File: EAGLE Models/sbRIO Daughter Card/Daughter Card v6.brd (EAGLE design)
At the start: 153.7 x 102.9 mm, 96 parts, among them IC1 BTS716G, IC2 BTS716G, IC3 BTS716G

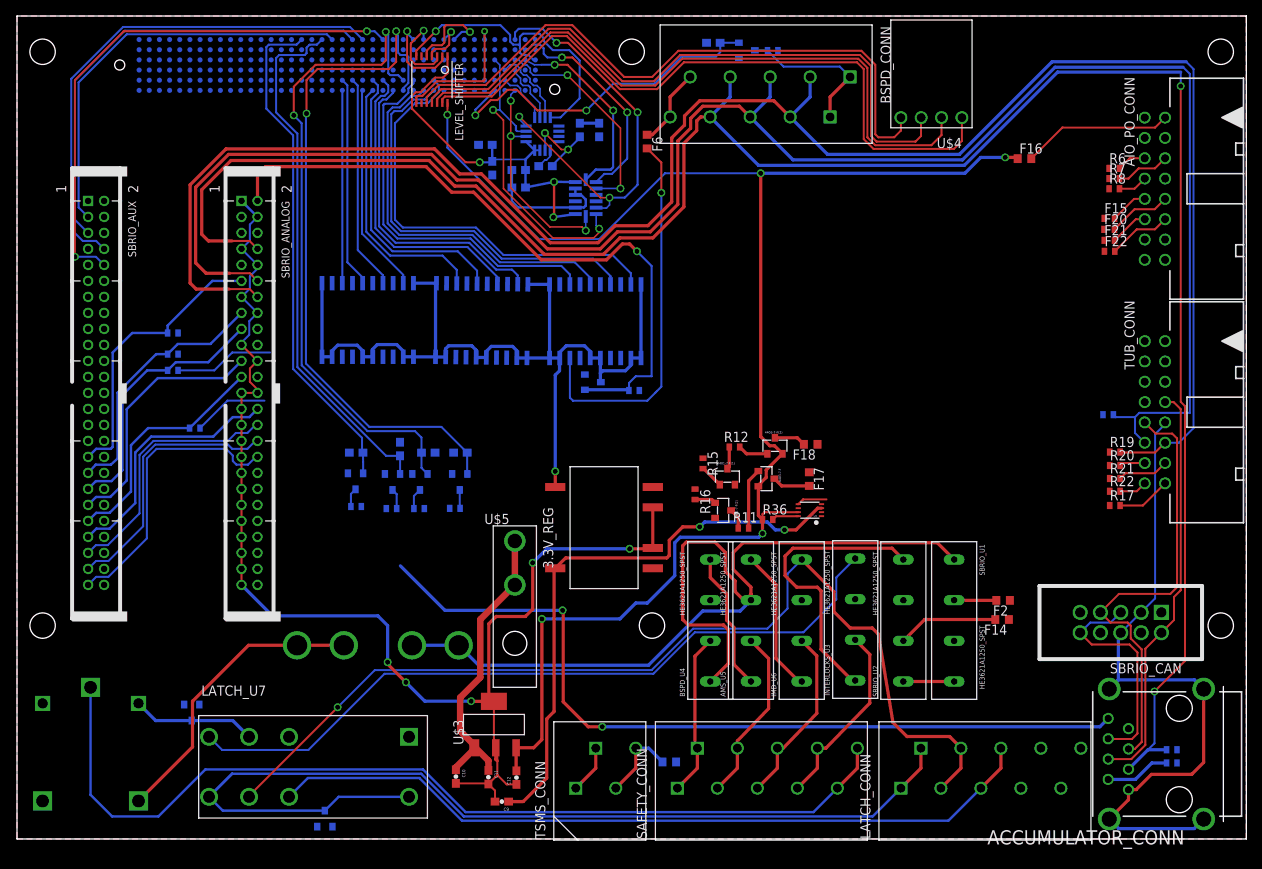
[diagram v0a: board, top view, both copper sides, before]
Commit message: traced ic's to right angle conn. and sorted resistors and began traces to ribon conn.
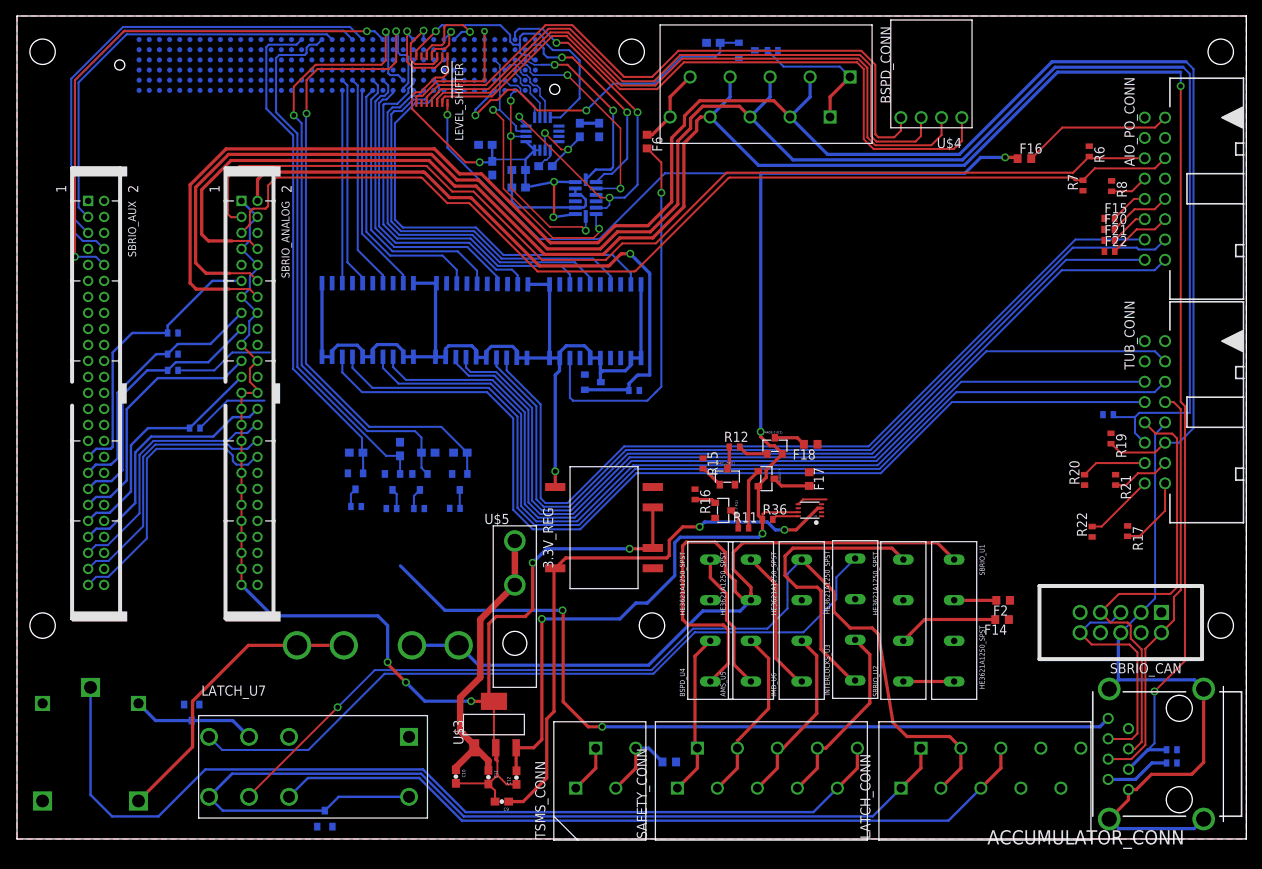
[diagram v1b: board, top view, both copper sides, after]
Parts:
- moved R22 5.80 mm to (134.4, 38.4), turned to 90 degrees
- moved R20 4.19 mm to (133.5, 44.9), turned to 90 degrees
- moved R7 4.01 mm to (133.2, 81.7), turned to 90 degrees
- moved R6 3.78 mm to (134.0, 86.0), turned to 270 degrees
- moved R17 3.58 mm to (138.8, 38.5), turned to 270 degrees
- moved R19 1.77 mm to (136.8, 50.1), turned to 270 degrees
- moved R8 0.47 mm to (136.8, 81.6), turned to 270 degrees
- moved R21 0.20 mm to (137.3, 44.9), turned to 270 degrees
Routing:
- net AI8: track 3.69 -> 131.9 mm
- net AMS_OUT: track 0.00 -> 125.2 mm
- net AI9: track 6.75 -> 131.6 mm
- net BUZZER_OUT: track 0.00 -> 123.7 mm
- net BSPD_OUT: track 0.00 -> 121.5 mm
- net IMD_OUT: track 0.00 -> 118.5 mm
- net ACCUMULATOR_FANS: track 0.00 -> 117.1 mm
- net PO2: track 0.00 -> 113.3 mm
- net PO3: track 0.00 -> 112.8 mm
- net PO4: track 0.00 -> 108.7 mm
- net AI7: track 3.49 -> 8.81 mm
- net THROTTLE_IN_1: track 3.21 -> 8.12 mm
- net STEERING_POS: track 38.6 -> 41.3 mm
- net N$4: track 83.2 -> 80.6 mm
- net BRAKE_PRESS_IN_2: track 235.6 -> 237.2 mm
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
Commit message: solved some tricky traces and continued resistor traces
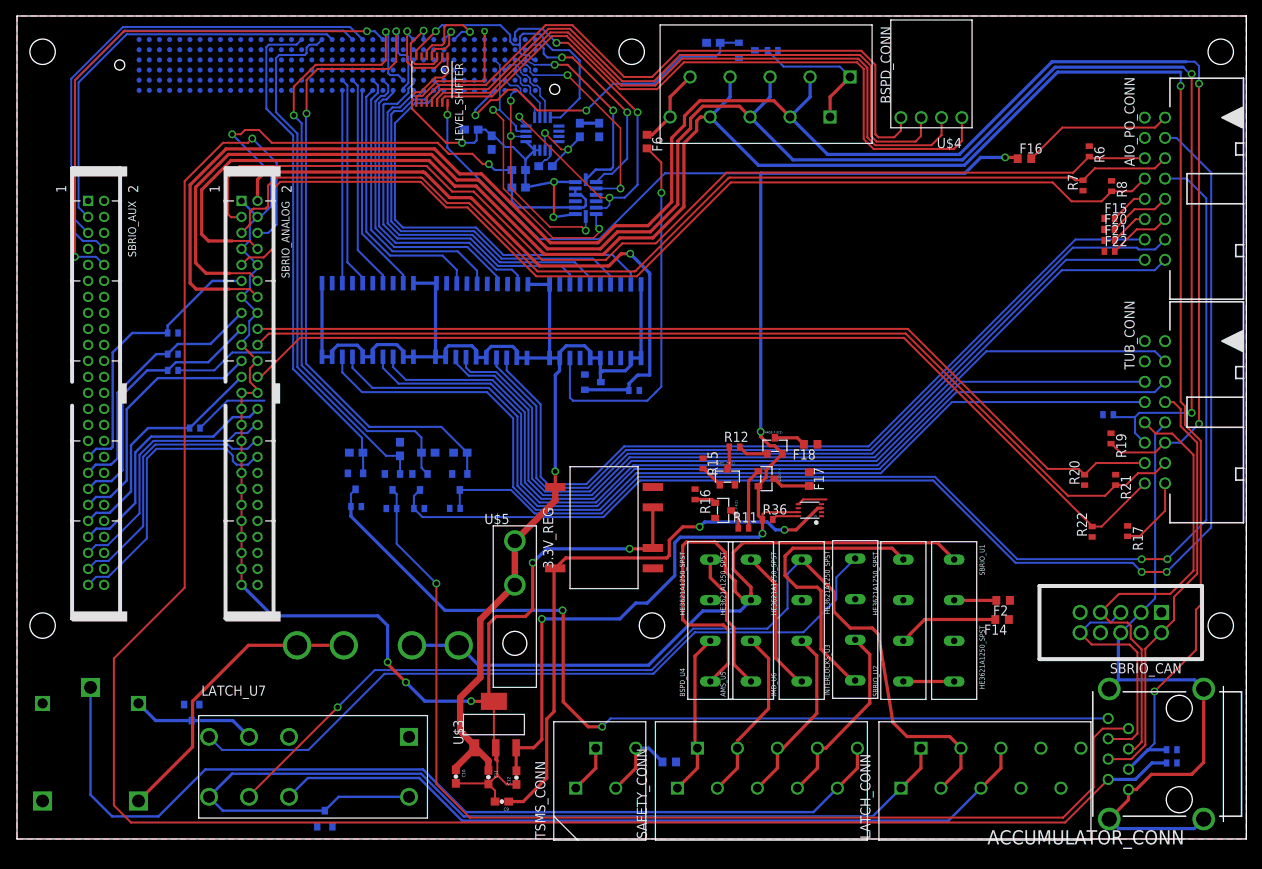
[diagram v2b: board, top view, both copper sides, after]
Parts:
- moved C6 3.20 mm to (59.3, 87.0)
- moved C5 2.59 mm to (56.8, 88.7)
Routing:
- net AI1: track 8.15 -> 242.7 mm, vias 0 -> 1
- net E-STOP_OK: track 2.64 -> 163.6 mm, vias 0 -> 2
- net LATCH_OK: track 2.32 -> 151.4 mm, vias 0 -> 2
- net AMS_OK_IN: track 2.54 -> 135.5 mm, vias 0 -> 1
- net AI10: track 4.80 -> 133.4 mm
- net THROTTLE_IN_2: track 7.31 -> 124.1 mm
- net AI7: track 8.81 -> 125.0 mm
- net THROTTLE_IN_1: track 8.12 -> 119.1 mm
- net DIO_GND: track 179.6 -> 230.1 mm, vias 5 -> 7
- net IMD_OK_IN: track 106.3 -> 116.3 mm
- net 12V: track 151.1 -> 160.0 mm
- net BUZZER_OUT: track 123.7 -> 120.0 mm
- net BSPD_OUT: track 121.5 -> 117.9 mm
- net AMS_OUT: track 125.2 -> 121.7 mm
- net PO2: track 113.3 -> 109.7 mm
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
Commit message: finished resistor traces
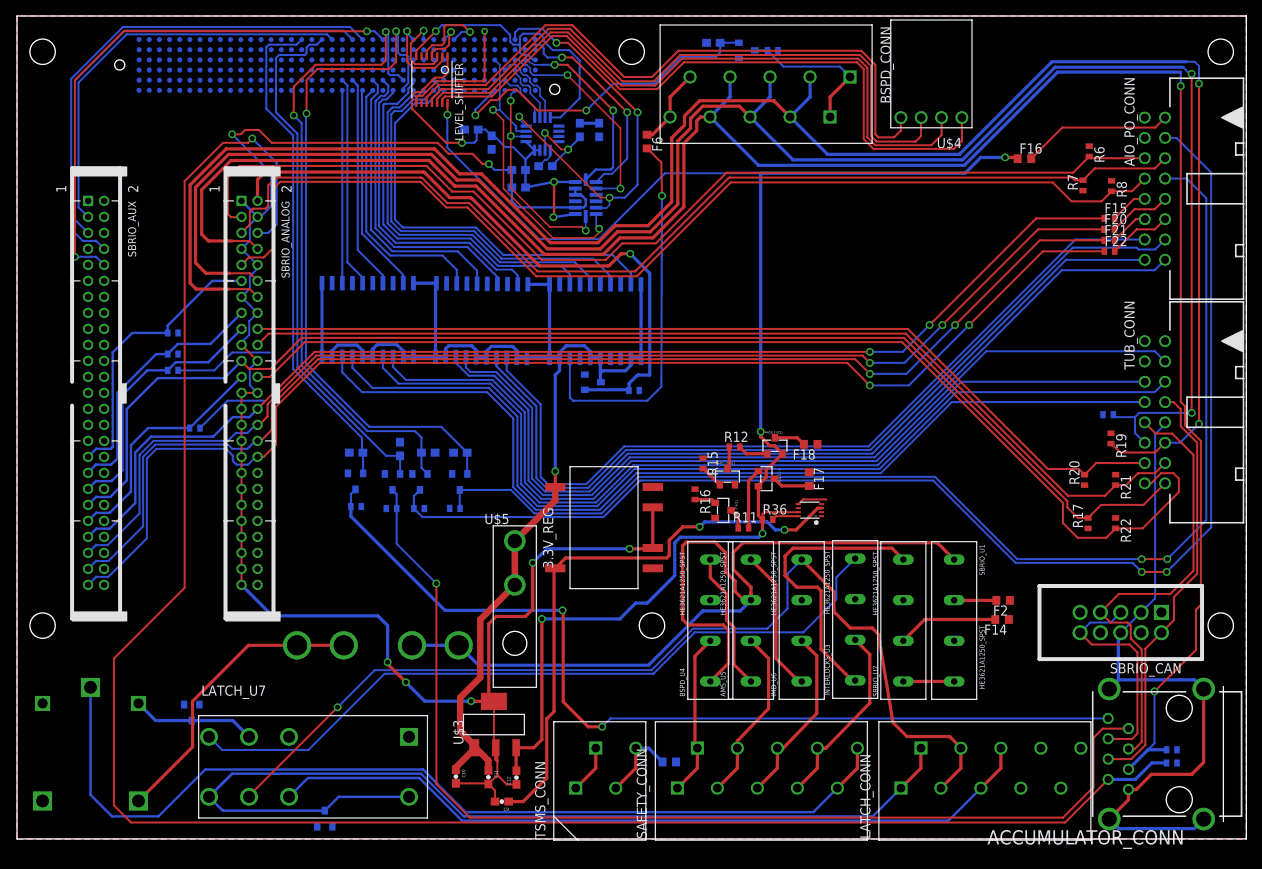
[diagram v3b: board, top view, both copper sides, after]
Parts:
- moved R17 5.05 mm to (133.9, 39.5), turned to 90 degrees
- moved R22 3.13 mm to (137.3, 39.5), turned to 270 degrees
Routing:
- net AO3: track 35.7 -> 157.3 mm, vias 0 -> 2
- net STEERING_POS: track 41.3 -> 160.9 mm
- net AO2: track 33.3 -> 152.9 mm, vias 0 -> 2
- net AO1: track 32.1 -> 149.7 mm, vias 0 -> 2
- net AO0: track 31.5 -> 147.2 mm, vias 0 -> 2
- net AI7: track 125.0 -> 137.7 mm

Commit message: Finished! some ground connections arent registering though
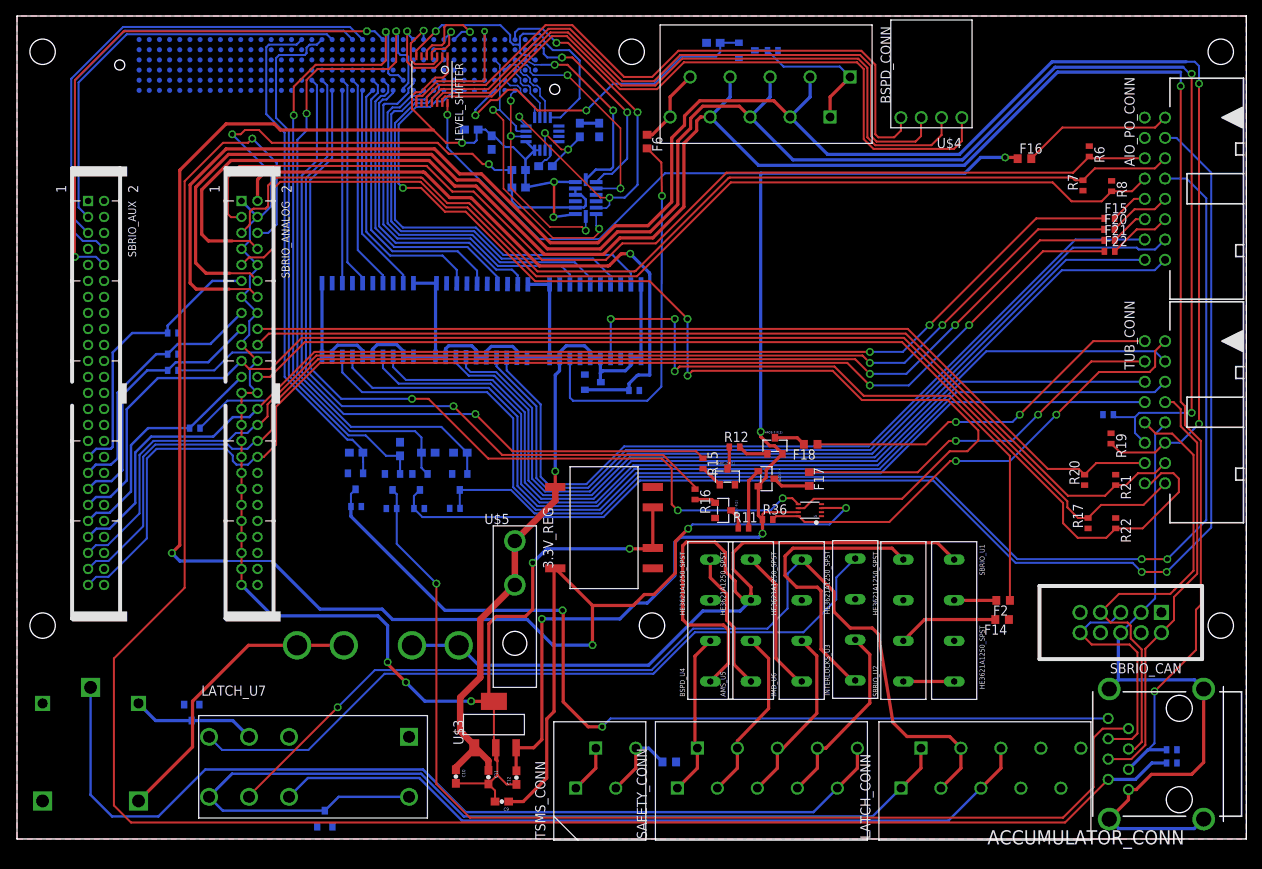
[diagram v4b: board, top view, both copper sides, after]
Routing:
- net 3.3V: track 120.0 -> 275.3 mm, vias 5 -> 7
- net DIO4: track 0.00 -> 133.2 mm, vias 0 -> 3
- net DIO12: track 3.78 -> 107.8 mm, vias 0 -> 3
- net DIO44: track 0.00 -> 92.6 mm, vias 0 -> 1
- net DIO45: track 0.00 -> 92.2 mm, vias 0 -> 1
- net SBRIO_OK+_1: track 0.00 -> 84.3 mm, vias 0 -> 3
- net LAP_TIMER_IN: track 3.36 -> 60.0 mm, vias 0 -> 2
- net 5V_IO_1: track 0.00 -> 47.7 mm, vias 0 -> 2
- net DC_DC_DISABLE: track 0.00 -> 46.3 mm, vias 0 -> 2
- net DIO7: track 87.6 -> 89.8 mm
- net DIO39: track 82.8 -> 84.2 mm
- net DIO94: track 66.5 -> 67.8 mm
- net DIO95: track 63.1 -> 63.6 mm

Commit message: DONE
finished board
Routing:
- net GND: vias 1 -> 7

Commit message: fixed the can lines to be more together and fixes the components on the bottom left to be on the top
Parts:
- moved U$8 16.4 mm to (9.65, 2.54), flipped to the top, turned to 90 degrees
- moved SBRIO_CAN 8.78 mm to (129.2, 26.2), turned to 270 degrees
- moved F2 1.07 mm to (122.2, 29.8)
- moved F14 0.91 mm to (122.2, 27.4)
- moved F3 0.23 mm to (45.3, 24.2), flipped to the top, turned to 270 degrees
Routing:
- net CAN_L: track 53.2 -> 75.2 mm
- net CAN_GND: track 84.8 -> 105.3 mm
- net CAN_H: track 57.7 -> 75.1 mm
- net TSMS_OUT+: track 119.8 -> 104.9 mm
- net N$14: track 37.1 -> 28.5 mm
- net TSMS_OUT_CTRL+: track 15.5 -> 22.3 mm
- net LATCH_SW_OUT: track 126.0 -> 124.4 mm
- net SBRIO_OK+_1_RELAY_IN: track 5.28 -> 4.22 mm
- net SBRIO_OK_2_RELAY: track 12.6 -> 11.7 mm

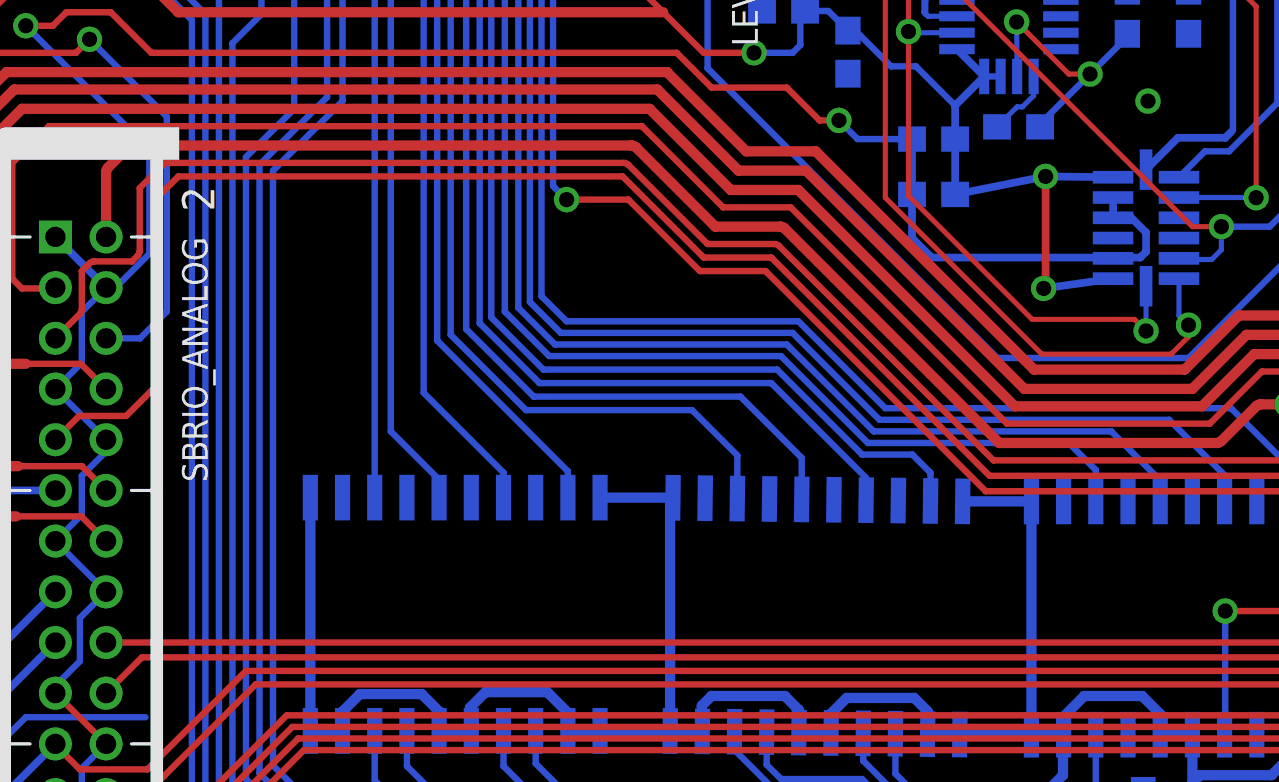
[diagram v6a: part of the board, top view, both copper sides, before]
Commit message: connected ground errors
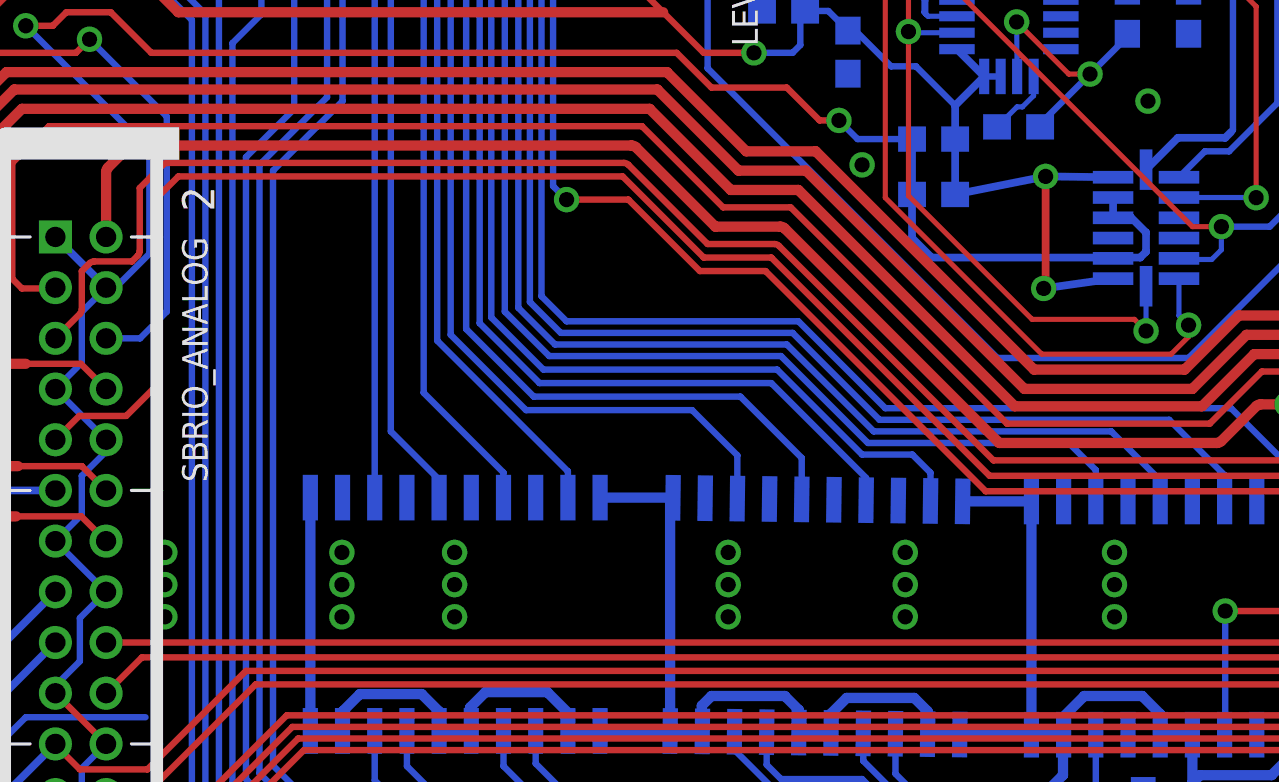
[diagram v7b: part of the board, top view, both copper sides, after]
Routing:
- net GND: vias 7 -> 26
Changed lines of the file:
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@@
 <via x="79.1718" y="56.9214" extent="1-16" drill="0.6"/>
 <via x="71.1708" y="85.1154" extent="1-16" drill="0.6"/>
-<wire x1="53.70133125" y1="69.449359375" x2="44.4754" y2="69.4716" width="0" layer="19" extent="16-16"/>
-<wire x1="67.8434" y1="69.3192" x2="58.780953125" y2="69.387296875" width="0" layer="19" extent="16-16"/>
-<wire x1="31.623" y1="60.8076" x2="39.3954" y2="69.4716" width="0" layer="19" extent="16-16"/>
+<via x="32.385" y="66.04" extent="1-16" drill="0.6"/>
+<via x="32.385" y="67.31" extent="1-16" drill="0.6"/>
+<via x="32.385" y="64.77" extent="1-16" drill="0.6"/>
+<via x="39.37" y="67.31" extent="1-16" drill="0.6"/>
+<via x="39.37" y="66.04" extent="1-16" drill="0.6"/>
+<via x="39.37" y="64.77" extent="1-16" drill="0.6"/>
+<via x="43.815" y="67.31" extent="1-16" drill="0.6"/>
+<via x="43.815" y="66.04" extent="1-16" drill="0.6"/>
+<via x="43.815" y="64.77" extent="1-16" drill="0.6"/>
+<via x="54.61" y="67.31" extent="1-16" drill="0.6"/>
+<via x="54.61" y="66.04" extent="1-16" drill="0.6"/>
+<via x="54.61" y="64.77" extent="1-16" drill="0.6"/>
+<via x="61.595" y="67.31" extent="1-16" drill="0.6"/>
+<via x="61.595" y="66.04" extent="1-16" drill="0.6"/>
+<via x="61.595" y="64.77" extent="1-16" drill="0.6"/>
+<via x="69.85" y="67.31" extent="1-16" drill="0.6"/>
+<via x="69.85" y="66.04" extent="1-16" drill="0.6"/>
+<via x="69.85" y="64.77" extent="1-16" drill="0.6"/>
+<via x="59.8932" y="82.6008" extent="1-16" drill="0.6"/>
 <wire x1="20.1318" y1="60.6044" x2="20.1318" y2="58.5724" width="0" layer="19" extent="16-16"/>
 <wire x1="20.1318" y1="63.246" x2="20.1318" y2="60.6044" width="0" layer="19" extent="16-16"/>
-<wire x1="65.2154" y1="84.0994" x2="59.3344" y2="86.1958" width="0" layer="19" extent="16-16"/>
+<wire x1="65.2154" y1="84.0994" x2="59.8932" y2="82.6008" width="0" layer="19" extent="16-16"/>
 <wire x1="136.8298" y1="82.2602" x2="134.0358" y2="86.6036" width="0" layer="19" extent="1-1"/>
 </signal>
@@
 <signal name="N$12">
 </signal>
+<signal name="N$15">
+</signal>
+<signal name="N$16">
+</signal>
+<signal name="N$17">
+</signal>
 </signals>
